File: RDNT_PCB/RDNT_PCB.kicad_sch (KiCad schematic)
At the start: 12 parts, among them U1 LT1117-ADJ

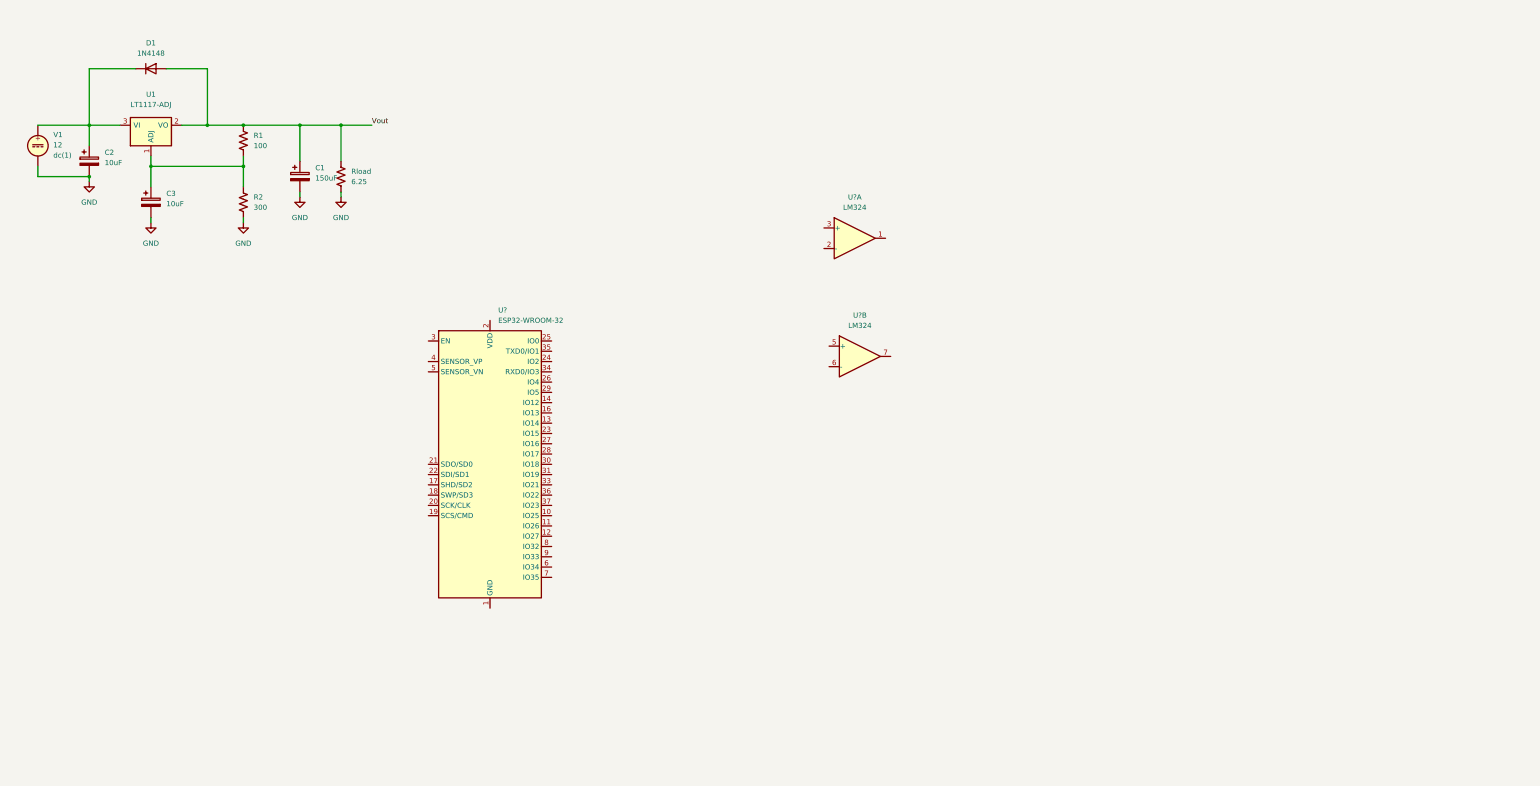
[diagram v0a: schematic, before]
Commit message: Updated schematic to current circuitry
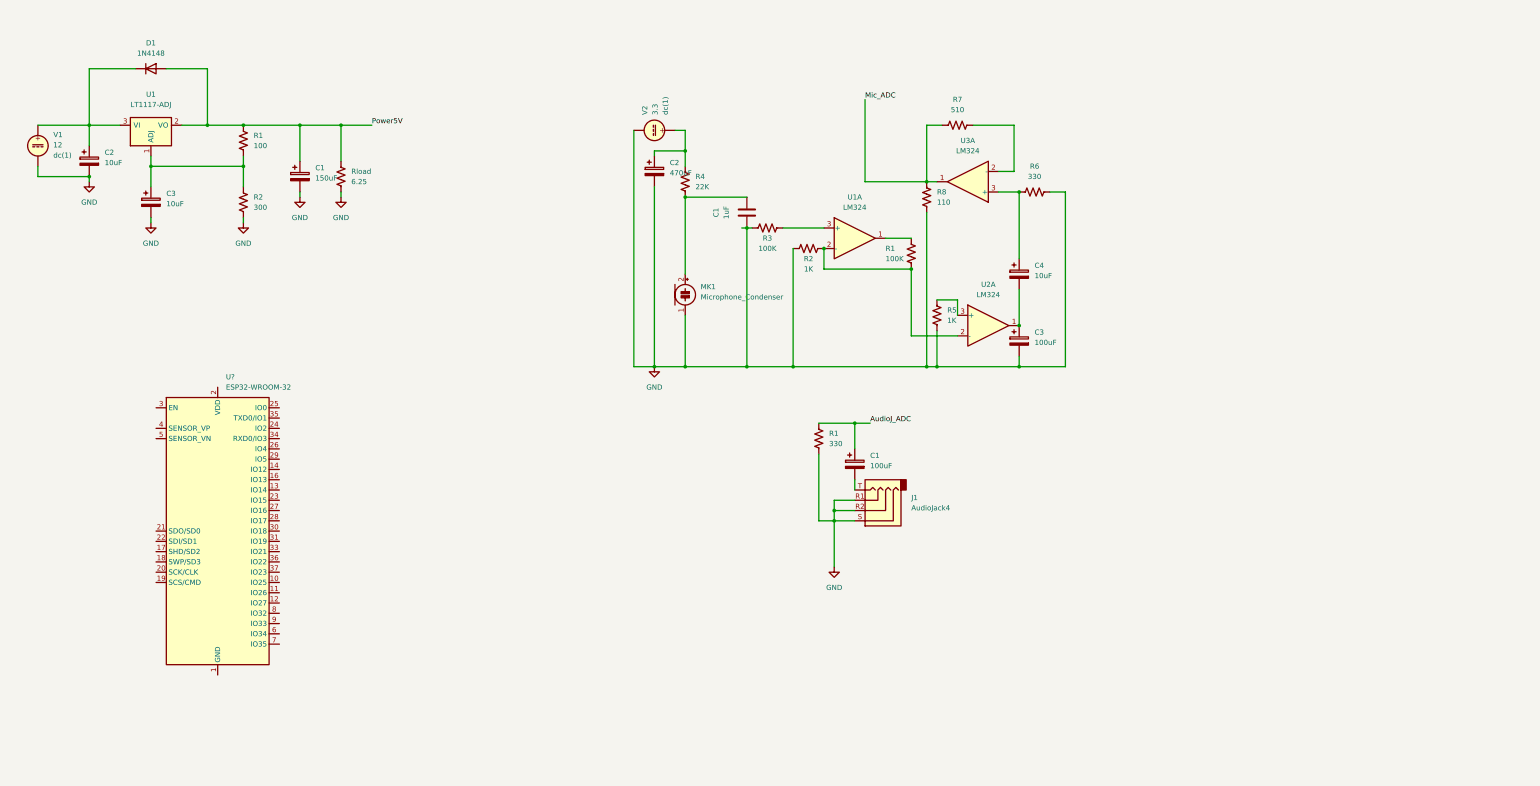
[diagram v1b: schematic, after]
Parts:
- added C1, C3: 100uF, symbol Device:C_Polarized
- added C1: 1uF, symbol Device:C
- added C2: 470uF, symbol Device:C_Polarized
- added C4: 10uF, symbol Device:C_Polarized
- added J1: AudioJack4, symbol Connector:AudioJack4
- added MK1: Microphone_Condenser, symbol Device:Microphone_Condenser
- added R1, R3: 100K, symbol Device:R_US
- added R1, R6: 330, symbol Device:R_US
- added R2, R5: 1K, symbol Device:R_US
- added R4: 22K, symbol Device:R_US
- added R7: 510, symbol Device:R_US
- added R8: 110, symbol Device:R_US
- added U3: LM324, symbol Amplifier_Operational:LM324
- added V2: 3.3, symbol Simulation_SPICE:VDC
- gave numbers to parts that had none: 2
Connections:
- net GND: now also C1.2, C2.2, C3.2, J1.R1, J1.R2, J1.S, MK1.1 (-), R1.2, R2.1, R3.1, R5.1, R6.2, R8.2, V2.2
- net at U1.1: now also R1.1
- net at U1.2 (-): now also U2.2 (-), R1.2, R2.2
- net at U1.3 (+): now also R3.2
- net Vout renamed Power5V
- new net: C4.1, R6.1, U3.3 (+)
- new net: C3.1, C4.2, U2.1
- new net: R7.2, U3.2 (-)
- new net: R5.2, U2.3 (+)
- new net: C1.2, J1.T
- new net: C1.1, MK1.2 (+), R4.1
- new net: C2.1, R4.2, V2.1
- new net AudioJ_ADC: C1.1, R1.1
- new net Mic_ADC: R7.1, R8.1, U3.1
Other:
- moved on the sheet: U2A, U?

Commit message: website updated pcb and presentation
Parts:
- removed C1: 150uF, symbol Device:C_Polarized
- removed C1: 100uF, symbol Device:C_Polarized
- removed C2, C3: 10uF, symbol Device:C_Polarized
- removed D1: 1N4148, Diode_THT:D_DO-35_SOD27_P7.62mm_Horizontal, symbol Diode:1N4148
- removed J1: AudioJack4, symbol Connector:AudioJack4
- removed MK1: Microphone_Condenser, symbol Device:Microphone_Condenser
- removed R1: 330, symbol Device:R_US
- removed R1: 100, symbol Device:R_US
- removed R2: 300, symbol Device:R_US
- removed Rload: 6.25, symbol Device:R_US
- removed U1: LT1117-ADJ, symbol Regulator_Linear:LT1117-ADJ
- removed U1, U2, U3: LM324, symbol Amplifier_Operational:LM324
- removed V1: 12, symbol Simulation_SPICE:VDC
- removed V2: 3.3, symbol Simulation_SPICE:VDC
- added C5: 100uF, Capacitor_SMD:C_1206_3216Metric, symbol Device:C_Polarized
- added C6, C8: .1uF, Capacitor_SMD:C_1206_3216Metric, symbol Device:C
- added C7: 0.1uF, Capacitor_SMD:C_1206_3216Metric, symbol Device:C
- added C_boot1, C_inx1: GRM155R71A104KA01D, TPS563300_Power_Circuit:C_Boot_CAPC1005X55N, symbol Power_Circuit_Lib:GRM155R71A104KA01D
- added C_in1: GRM31CR71E106KA12L, TPS563300_Power_Circuit:C_IN_CAPC3216X180N, symbol Power_Circuit_Lib:GRM31CR71E106KA12L
- added C_out1: GRM32EC80J107ME20L, TPS563300_Power_Circuit:C_OUT_CAPC3225X270N, symbol Power_Circuit_Lib:GRM32EC80J107ME20L
- added H1, H2, H3, H4: MountingHole, MountingHole:MountingHole_3.2mm_M3, symbol Mechanical:MountingHole
- added IC1: TPS563300DRLR, TPS563300_Power_Circuit:TPS563300DRLR, symbol TPS563300 Power Circuit:TPS563300DRLR
- added J1, J2: AudioJack3, Connector_Audio:Jack_3.5mm_CUI_SJ-3523-SMT_Horizontal, symbol Connector:AudioJack3
- added J3: Conn_02x05_Counter_Clockwise, Connector_PinHeader_2.00mm:PinHeader_2x05_P2.00mm_Vertical_SMD, symbol Connector_Generic:Conn_02x05_Counter_Clockwise
- added L1: HCM0703-4R7-R, TPS563300_Power_Circuit:L1_HCM0703-4R7-R, symbol Power_Circuit_Lib:HCM0703-4R7-R
- added MK1: CMA-4544PF-W, electret_mic:MIC_CMA-4544PF-W, symbol electret_mic:CMA-4544PF-W
- added R10: 68K, Resistor_SMD:R_1206_3216Metric, symbol Device:R_US
- added R11: 330, Resistor_SMD:R_1206_3216Metric, symbol Device:R_US
- added R12: 510, Resistor_SMD:R_1206_3216Metric, symbol Device:R_US
- added R13, R9: 1K, Resistor_SMD:R_1206_3216Metric, symbol Device:R_US
- added R_fbb1: CRCW040210K0FKED, TPS563300_Power_Circuit:R_FBB_RESC1005X40N, symbol Power_Circuit_Lib:CRCW040210K0FKED
- added R_fbt1: CRCW060330K9FKEA, TPS563300_Power_Circuit:R_FBT_RESC1508X50N, symbol Power_Circuit_Lib:CRCW060330K9FKEA
- added SW1: SW_MEC_5E, Button_Switch_SMD:SW_MEC_5GSH9, symbol Switch:SW_MEC_5E
- added U1: TMUX1309QDYYRQ1, TMUX1309QDYYRQ1:TMUX1309QDYYRQ1, symbol TMUX1309QDYYRQ1:TMUX1309QDYYRQ1
- added U6: LM324, Package_SO:SOIC-14_3.9x8.7mm_P1.27mm, symbol Amplifier_Operational:LM324
- C1, C2, C3, C4: footprint (none) -> Capacitor_SMD:C_1206_3216Metric
- R1, R2, R3, R4, R5, R8: footprint (none) -> Resistor_SMD:R_1206_3216Metric
- R6: value 330 -> 87; footprint (none) -> Resistor_SMD:R_1206_3216Metric
- R7: value 510 -> 390; footprint (none) -> Resistor_SMD:R_1206_3216Metric
- gave numbers to parts that had none: 1
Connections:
- net Mic_ADC: now also C7.1, J3.6 (Pin_6), R12.2, U1.14 (S1); no longer R7.1, R8.1
- net at C4.1: now also C3.1, U6.7; no longer R6.1
- net at C4.2: now also R6.1, U6.10 (+); no longer C3.1
- net at R7.2: now also R8.1, U6.9 (-)
- net at R1.1: now also U6.1
- net at R1.2, R2.2: now also U6.2 (-), U6.6 (-)
- net at R5.2: now also R10.1, U6.5 (+)
- net GNDREF: now reaches U2.1 (GND), U2.15 (GND), U2.38 (GND), U2.39 (GND)
- net GNDREF: now also C2.2, C3.2, R2.1, R3.1, R5.1, R6.2, R8.2, C6.1, C7.2, C8.1, C_in1.2, C_inx1.2, C_out1.2, IC1.4 (GND), J1.S, J2.R, J2.S, MK1.1, R11.2, R9.1, R_fbb1.1, U1.8 (GND), U6.11 (V-)
- net Ble_DAC: now reaches U2.10 (IO25)
- net Ble_DAC: now also J3.4 (Pin_4), U1.12 (S3)
- net VCC: now reaches U2.2 (VDD)
- net VCC: now also C2.1, R4.2, C6.2, C_out1.1, J3.2 (Pin_2), L1.1, R10.2, R13.1, R_fbt1.2, U1.16 (VDD), U6.4 (V+)
- net mode: now reaches U2.28 (IO17)
- net mode: now also J3.9 (Pin_9), SW1.4 (A)
- net sel1: now reaches U2.30 (IO18)
- net sel1: now also J3.8 (Pin_8), U1.11 (A0)
- net sel2: now reaches U2.31 (IO19)
- net sel2: now also J3.7 (Pin_7), U1.10 (A1)
- net Mux_Out: now reaches U2.6 (IO34)
- net Mux_Out: now also J1.R, J1.T, J3.3 (Pin_3), U1.3 (D)
- net LED_Out: now reaches U2.9 (IO33)
- net LED_Out: now also J3.10 (Pin_10)
- net at R3.2: now also C1.2, MK1.2, U6.3 (+)
- removed net GND: C1.2, C2.2, C3.2, R2.1, R3.1, R5.1, R6.2, R8.2
- new net: C_boot1.2, IC1.5 (SW), L1.2
- new net: C5.2, J2.T
- new net: IC1.8 (FB), R_fbb1.2, R_fbt1.1
- new net: R12.1, R7.1, U6.8
- new net: C8.2, R13.2, SW1.1
- new net: C_boot1.1, IC1.6 (BST)
- new net: R9.2, SW1.2
- new net +5V: C_in1.1, C_inx1.1, IC1.3 (VIN), J3.1 (Pin_1)
- new net Aux_ADC: C5.1, J3.5 (Pin_5), R11.1, U1.15 (S2)
- no-connect marks 0 -> 41
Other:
- moved on the sheet: C1, C2, C3, C4, R1, R2, R3, R4, R5, R6, R7, R8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

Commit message: PCB Updated
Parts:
- removed C2: 470uF, Capacitor_SMD:C_1206_3216Metric, symbol Device:C_Polarized
- removed C3, C5: 100uF, Capacitor_SMD:C_1206_3216Metric, symbol Device:C_Polarized
- removed C4: 10uF, Capacitor_SMD:C_1206_3216Metric, symbol Device:C_Polarized
- removed H1: MountingHole, MountingHole:MountingHole_3.2mm_M3, symbol Mechanical:MountingHole
- removed J3: Conn_02x05_Counter_Clockwise, Connector_PinHeader_2.00mm:PinHeader_2x05_P2.00mm_Vertical_SMD, symbol Connector_Generic:Conn_02x05_Counter_Clockwise
- removed MK1: CMA-4544PF-W, electret_mic:MIC_CMA-4544PF-W, symbol electret_mic:CMA-4544PF-W
- removed R10: 68K, Resistor_SMD:R_1206_3216Metric, symbol Device:R_US
- removed R11: 330, Resistor_SMD:R_1206_3216Metric, symbol Device:R_US
- removed R13, R5: 1K, Resistor_SMD:R_1206_3216Metric, symbol Device:R_US
- removed R4: 22K, Resistor_SMD:R_1206_3216Metric, symbol Device:R_US
- removed R6: 87, Resistor_SMD:R_1206_3216Metric, symbol Device:R_US
- removed U1: TMUX1309QDYYRQ1, TMUX1309QDYYRQ1:TMUX1309QDYYRQ1, symbol TMUX1309QDYYRQ1:TMUX1309QDYYRQ1
- removed U2: ESP32-WROOM-32, RF_Module:ESP32-WROOM-32, symbol RF_Module:ESP32-WROOM-32
- removed U6: LM324, Package_SO:SOIC-14_3.9x8.7mm_P1.27mm, symbol Amplifier_Operational:LM324
- added C10, C3, C9: 10uF, Capacitor_SMD:C_1206_3216Metric, symbol Device:C
- added C11, C12, C2, C4, C5: 0.1uF, Capacitor_SMD:C_1206_3216Metric, symbol Device:C
- added H5: MountingHole, MountingHole:MountingHole_3.2mm_M3, symbol Mechanical:MountingHole
- added J1: Conn_ARM_JTAG_SWD_10, Connector_PinHeader_1.27mm:PinHeader_2x05_P1.27mm_Vertical_SMD, symbol Connector:Conn_ARM_JTAG_SWD_10
- added J2: Conn_01x07_Male, symbol Connector:Conn_01x07_Male
- added J4: Conn_01x03_Male, symbol Connector:Conn_01x03_Male
- added J5, J6: Screw_Terminal_01x03, Connector_PinHeader_2.54mm:PinHeader_1x03_P2.54mm_Vertical, symbol Connector:Screw_Terminal_01x03
- added MK2: CMA-4544PF-W, electret_mic:MIC_CMA-4544PF-W, symbol electret_mic:CMA-4544PF-W
- added R15: 10K, Resistor_SMD:R_1206_3216Metric, symbol Device:R_US
- added R17: 2200, Resistor_SMD:R_1206_3216Metric, symbol Device:R_US
- added R18: 400000, Resistor_SMD:R_1206_3216Metric, symbol Device:R_US
- added R19: 100000, Resistor_SMD:R_1206_3216Metric, symbol Device:R_US
- added R20: 1000, Resistor_SMD:R_1206_3216Metric, symbol Device:R_US
- added R21: 1500, Resistor_SMD:R_1206_3216Metric, symbol Device:R_US
- added SW2, SW3: SW_MEC_5E, Button_Switch_SMD:SW_MEC_5GSH9, symbol Switch:SW_MEC_5E
- added U1: ESP32-WROOM-32D, RF_Module:ESP32-WROOM-32, symbol RF_Module:ESP32-WROOM-32D
- added U2: PTMUX1308QDYYRQ1, TMUX1309QDYYRQ1:PTMUX1308QDYYRQ1, symbol TMUX:PTMUX1308QDYYRQ1
- added U3: LM324, Lm324:LM324D, symbol Amplifier_Operational:LM324
- C1: value 1uF -> 0.1uF
- C7: value 0.1uF -> 1uF
- C8: value .1uF -> 0.033uF
- R1: value 100K -> 10K
- R12: value 510 -> 1K
- R2, R9: value 1K -> 10K
- R3: value 100K -> 1
- R7: value 390 -> 203K
- R8: value 110 -> 100K
- renumbered J1 to J_in1, J2 to J_out1
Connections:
- net +5V: now also C6.2, IC1.2 (EN), R7.1, C11.1, J5.2 (Pin_2), J6.2 (Pin_2), U2.16 (VDD), U3.4 (V+)
- net Ble_DAC: now also U1.10 (IO25), U2.15 (S2)
- net VCC: now also R1.1, R2.1, R9.1, SW1.3 (K), SW1.4 (A), C2.2, C3.2, C5.1, J1.1 (VTref), R15.1, R17.1, R18.1, U1.2 (VDD); no longer C6.2
- net mode: now also R12.2, C4.2; no longer SW1.4 (A)
- net sel1: now also U1.30 (IO18), U2.11 (A0)
- net sel2: now also U1.31 (IO19), U2.10 (A1)
- net DGND: now reaches R2.2
- net DGND: now also C1.2, C_in1.2, C_inx1.2, C_out1.2, IC1.4 (GND), R3.2, R_fbb1.1, C12.2, C2.1, C3.1, C4.1, J1.3 (GND), J1.5 (GND), J1.9 (GNDDetect), J4.3 (Pin_3), J5.1 (Pin_1), J6.1 (Pin_1), SW2.1, SW2.2, SW3.1, SW3.2, U1.1 (GND), U1.15 (GND), U1.38 (GND), U1.39 (GND); no longer R1.2
- net ADC_In: now reaches J_out1.T
- net ADC_In: now also J_out1.R, U1.6 (IO34), U2.3 (D)
- net at R12.1: now also SW1.1, SW1.2, C5.2; no longer R7.1
- net Mic_out: now reaches C8.2
- net Mic_out: now also R21.1, U2.13 (S0), U3.14; no longer SW1.1
- net at R9.2: now also J1.10 (~{RESET}); no longer SW1.2
- net reset: now reaches C1.1
- net reset: now also R15.2, SW2.3 (K), SW2.4 (A), U1.3 (EN)
- net at R7.2, R8.1: now also C10.1, C9.1, U3.5 (+)
- removed net GNDREF: C6.1, C7.2, C8.1, C_in1.2, C_inx1.2, C_out1.2, IC1.4 (GND), J_in1.S, J_out1.R, J_out1.S, R2.1, R3.1, R8.2, R9.1, R_fbb1.1
- net Mic_ADC: no longer names the net of C7.1
- net Mic_ADC: now also MK2.1, R17.2; no longer R12.2
- net Mux_Out: no longer names the net of J_in1.T
- net Mux_Out: now also C10.2; no longer J_in1.R
- new net: C7.2, R18.2, R19.2, U3.12 (+)
- new net: C8.1, R20.2, R21.2, U3.13 (-)
- new net: U3.1, U3.2 (-)
- new net: J1.2 (SWDIO/TMS), U1.13 (IO14)
- new net: J1.8 (NC/TDI), U1.14 (IO12)
- new net: J1.4 (SWDCLK/TCK), U1.16 (IO13)
- new net: J1.6 (SWO/TDO), U1.23 (IO15)
- new net: C9.2, J_in1.R
- new net: U3.8, U3.9 (-)
- new net ADC_backup: J2.1 (Pin_1), U1.7 (IO35)
- new net AGND: C11.2, C6.1, J_in1.S, J_out1.S, MK2.2, R19.1, R20.1, R3.1, R8.2, U2.1 (S4), U2.12 (S3), U2.2 (S6), U2.4 (S7), U2.5 (S5), U2.6 (EN), U2.8 (GND), U2.9 (A2), U3.10 (+), U3.11 (V-), U3.3 (+)
- new net AUX_mono: U2.14 (S1), U3.6 (-), U3.7
- new net Case_LED: J5.3 (Pin_3), U1.36 (IO22)
- new net Case_backup: J2.4 (Pin_4), U1.37 (IO23)
- new net DAC_backup: J2.2 (Pin_2), U1.11 (IO26)
- new net LED_backup: J2.3 (Pin_3), U1.27 (IO16)
- new net LED_out: J6.3 (Pin_3), U1.26 (IO4)
- new net Mode_backup: J2.5 (Pin_5), U1.8 (IO32)
- new net Mode_sel: U1.12 (IO27)
- new net Rx: J4.2 (Pin_2), U1.34 (RXD0/IO3)
- new net Tx: J4.1 (Pin_1), U1.35 (TXD0/IO1)
- new net boot: C12.1, R1.2, SW3.3 (K), SW3.4 (A), U1.25 (IO0)
- new net sel1_backup: J2.6 (Pin_6), U1.29 (IO5)
- new net sel2_backup: J2.7 (Pin_7), U1.28 (IO17)
- no-connect marks 41 -> 2
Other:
- moved on the sheet: C6, C_boot1, C_in1, C_inx1, C_out1, H2, H3, H4, IC1, J_in1, J_out1, L1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

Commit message: zipped grb drl
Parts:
- removed R9: 10K, Resistor_SMD:R_1206_3216Metric, symbol Device:R_US
- added C13: .01uF, Capacitor_SMD:C_1206_3216Metric, symbol Device:C
- added R4: 500, Resistor_SMD:R_1206_3216Metric, symbol Device:R_US
- J5, J6: footprint Connector_PinHeader_2.54mm:PinHeader_1x03_P2.54mm_Vertical -> Connector_Phoenix_MSTB:PhoenixContact_MSTBA_2,5_3-G-5,08_1x03_P5.08mm_Horizontal
- R12: value 1K -> 100
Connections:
- net ADC_In: now also C13.2, R4.1; no longer U2.3 (D)
- net AGND: now also C13.1
- net DGND: now also J6.3 (Pin_3); no longer J6.1 (Pin_1)
- net LED_out: now also J6.1 (Pin_1); no longer J6.3 (Pin_3)
- net VCC: no longer R2.1
- net mode: now also R2.1
- net reset: now also J1.10 (~{RESET})
- new net: R4.2, U2.3 (D)
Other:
- moved on the sheet: R2
